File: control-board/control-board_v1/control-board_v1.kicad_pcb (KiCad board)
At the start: 2 copper layers, 68.6 x 53.3 mm, 59 parts, among them J1 Barrel_Jack, J2 PH2-12-UA, J3 PH2-12-UA, J4 PH2-12-UA, J5 PH2-12-UA, J6 Conn_01x08_Socket, J7 Conn_01x06_Socket, J8 Conn_01x10_Socket, J9 Conn_01x08_Socket, Q1 Q_Dual_NMOS_S1G1D2S2G2D1, Q2 Q_Dual_NMOS_S1G1D2S2G2D1, Q3 Q_Dual_NMOS_S1G1D2S2G2D1, Q4 Q_Dual_NMOS_S1G1D2S2G2D1, Q5 Q_Dual_NMOS_S1G1D2S2G2D1, Q6 Q_Dual_NMOS_S1G1D2S2G2D1, Q7 Q_Dual_NMOS_S1G1D2S2G2D1, Q8 Q_Dual_NMOS_S1G1D2S2G2D1, U1 CD74HCT154M, U2 SN74HC540DWR, U3 SN74HC540DWR

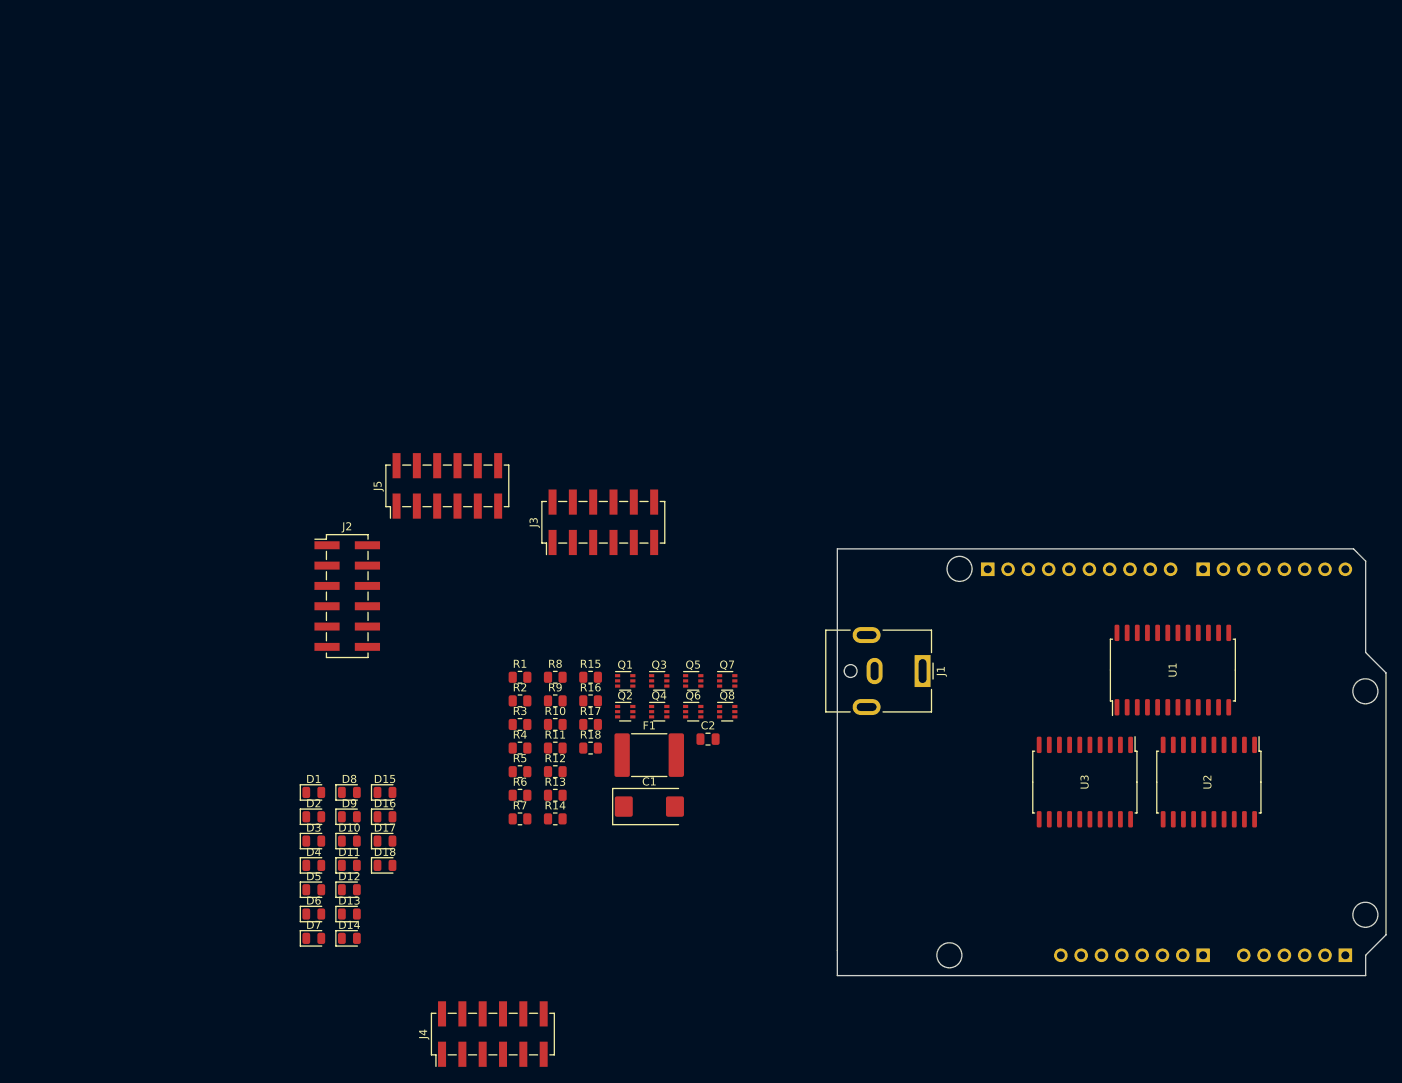
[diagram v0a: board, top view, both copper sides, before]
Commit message: added pcb layout
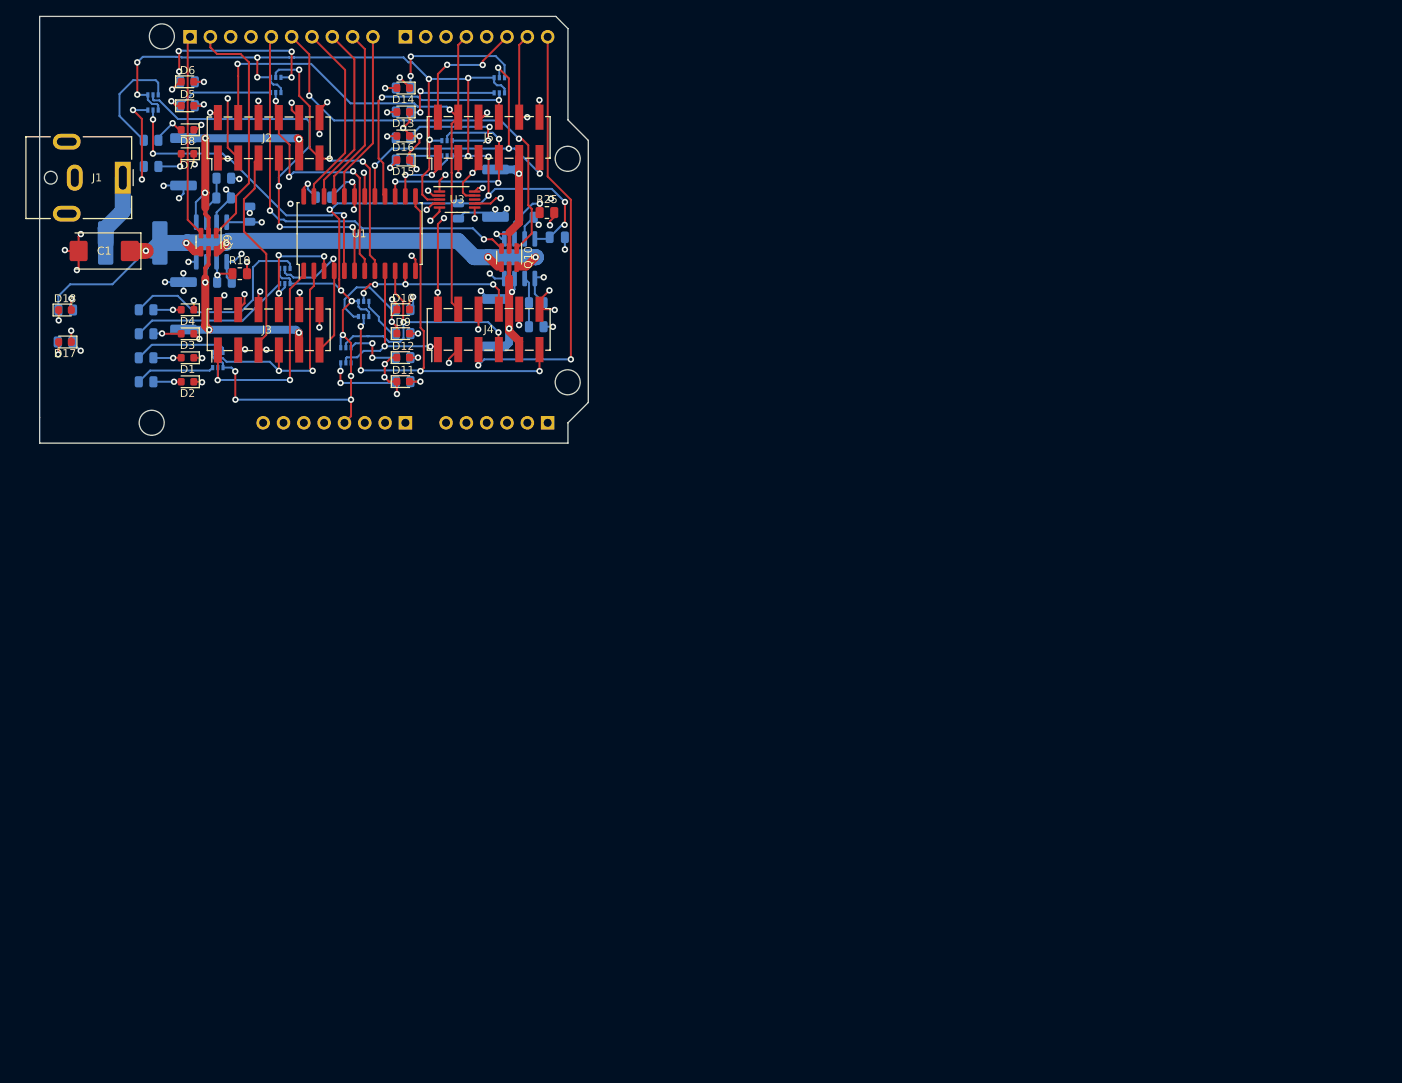
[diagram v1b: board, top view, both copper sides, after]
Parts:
- removed U2: SN74HC540DWR, Package_SO:SOIC-20W_7.5x12.8mm_P1.27mm
- added C3: 0.1uF, Capacitor_SMD:C_0805_2012Metric, B.Cu at (81.5, 42.9)
- added C5: 0.1uF, Capacitor_SMD:C_0805_2012Metric, B.Cu at (69.2, 39.6)
- added C7: 0.1uF, Capacitor_SMD:C_0805_2012Metric, B.Cu at (43.1, 40.0)
- added Q10: NMOS, Package_TO_SOT_SMD:SOT-23-6, F.Cu at (75.5, 45.4)
- added Q9: NMOS, Package_TO_SOT_SMD:SOT-23-6, F.Cu at (38.0, 43.5)
- added R19: 100, Resistor_SMD:R_0805_2012Metric, F.Cu at (41.9, 47.5)
- added R20: 166K, Resistor_SMD:R_0805_2012Metric, B.Cu at (40.0, 48.5)
- added R21: 100, Resistor_SMD:R_0805_2012Metric, B.Cu at (39.9, 35.5)
- added R22: 166K, Resistor_SMD:R_0805_2012Metric, B.Cu at (39.9, 38.0)
- added R23: 0.003, Resistor_SMD:R_2512_6332Metric, B.Cu at (73.8, 53.6)
- added R24: 0.003, Resistor_SMD:R_2512_6332Metric, B.Cu at (73.8, 37.4)
- added R25: 100, Resistor_SMD:R_0805_2012Metric, F.Cu at (80.3, 39.8)
- added R26: 100, Resistor_SMD:R_0805_2012Metric, B.Cu at (78.9, 54.1)
- added R27: 166K, Resistor_SMD:R_0805_2012Metric, B.Cu at (77.7, 40.4)
- added R28: 166K, Resistor_SMD:R_0805_2012Metric, B.Cu at (78.9, 51.1)
- added R42: 0.003, Resistor_SMD:R_2512_6332Metric, B.Cu at (34.8, 51.5)
- added R47: 0.003, Resistor_SMD:R_2512_6332Metric, B.Cu at (34.8, 33.5)
- added U4: Opamp_Dual, Package_SO:SOIC-8_3.9x4.9mm_P1.27mm, B.Cu at (38.3, 43.5)
- added U6: Opamp_Dual, Package_SO:SOIC-8_3.9x4.9mm_P1.27mm, B.Cu at (76.8, 45.6)
- C2, R1, R10, R11, R12, R13, R14, R15, R16, R18, R2, R3, R4, R5, R6, R7, R8, R9: moved to B.Cu
- D1, D17, D2, D3, D4: footprint LED_SMD:LED_0805_2012Metric -> LED_SMD:LED_0603_1608Metric
- D10, D11, D12, D9: value BLUE LED -> RED LED; footprint LED_SMD:LED_0805_2012Metric -> LED_SMD:LED_0603_1608Metric
- D13, D14, D15, D16: value BLUE LED -> YELLOW LED; footprint LED_SMD:LED_0805_2012Metric -> LED_SMD:LED_0603_1608Metric
- D18: value RED LED -> ORANGE LED; footprint LED_SMD:LED_0805_2012Metric -> LED_SMD:LED_0603_1608Metric
- D5, D6, D7, D8: value BLUE LED -> WHITE LED; footprint LED_SMD:LED_0805_2012Metric -> LED_SMD:LED_0603_1608Metric
- F1: value 0ZCF0125FF2C -> Bell_Fuse; moved to B.Cu
- J2, J3, J4, J5: value PH2-12-UA -> Header-M_2x6
- J6, J9: value Conn_01x08_Socket -> Header_1x8
- J7: value Conn_01x06_Socket -> Header_1x8
- J8: value Conn_01x10_Socket -> Header_1x10
- Q1, Q2, Q3, Q4, Q5, Q6, Q7, Q8: value Q_Dual_NMOS_S1G1D2S2G2D1 -> PMOS; moved to B.Cu
- R17: value 1K -> 100; moved to B.Cu
- U3: value SN74HC540DWR -> ADS1118; footprint Package_SO:SOIC-20W_7.5x12.8mm_P1.27mm -> Package_SO:VSSOP-10_3x3mm_P0.5mm
- moved J6 119.9 mm to (62.6, 66.1)
- moved J7 119.9 mm to (80.3, 66.1)
- moved J8 119.9 mm to (35.6, 17.8)
- moved J9 119.9 mm to (62.6, 17.8)
- moved J1 117.5 mm to (27.2, 35.5)
- moved U1 115.4 mm to (56.8, 42.4)
- moved U3 107.1 mm to (69.0, 38.2), turned to 0 degrees
- moved D14 106.5 mm to (62.3, 24.2), turned to 180 degrees
- moved D6 105.2 mm to (35.3, 23.5)
- moved D13 100.5 mm to (62.3, 27.2), turned to 180 degrees
- moved D7 99.3 mm to (35.3, 32.5), turned to 180 degrees
- moved D5 99.3 mm to (35.3, 26.5)
- moved Q4 99.0 mm to (31.0, 26.1), turned to 90 degrees
- moved R6 98.4 mm to (35.3, 23.5)
- moved C1 97.3 mm to (24.9, 44.6), turned to 180 degrees
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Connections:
- net D10 renamed S-D10
- net D11 renamed S-D11
- net D8 renamed S-D8
- net D9 renamed S-D9
- C2 pad 2: +5V -> +3V3
- D1 pad 1: Net-(D1-K) -> GND
- D10 pad 1: Net-(D10-K) -> GND
- D11 pad 1: Net-(D11-K) -> GND
- D12 pad 1: Net-(D12-K) -> GND
- D13 pad 1: Net-(D13-K) -> GND
- D14 pad 1: Net-(D14-K) -> GND
- D15 pad 1: Net-(D15-K) -> GND
- D16 pad 1: Net-(D16-K) -> GND
- D2 pad 1: Net-(D2-K) -> GND
- D3 pad 1: Net-(D3-K) -> GND
- D4 pad 1: Net-(D4-K) -> GND
- D5 pad 1: Net-(D5-K) -> GND
- D6 pad 1: Net-(D6-K) -> GND
- D7 pad 1: Net-(D7-K) -> GND
- D8 pad 1: Net-(D8-K) -> GND
- D9 pad 1: Net-(D9-K) -> GND
- J1 pad MP: (no net) -> GND
- J2 pad 9: +9V -> 2-Heater
- J3 pad 9: +9V -> 1-Heater
- J4 pad 9: +9V -> 3-Heater
- J5 pad 5: unconnected-(J5-Pin_5-Pad5) -> DOUT
- J5 pad 9: +9V -> 4-Heater
- J8 pad 1: SCL -> H2-D13
- J8 pad 2: SDA -> H1-D12
- J8 pad 5: D13 -> H4-D19
- J8 pad 6: D12 -> H3-D18
- J9 pad 2: D6 -> ~{ENABLE}
- J9 pad 5: D3 -> CS
- J9 pad 6: CLK -> DIN
- J9 pad 7: DIN -> CLK
- Q1 pad 1: Inv_4T1 -> +5V
- Q1 pad 2: GND -> 1-CS
- Q1 pad 3: Net-(D2-K) -> Net-(Q1B-D)
- Q1 pad 4: Inv_4 -> +5V
- Q1 pad 5: GND -> 1-CS_T1
- Q1 pad 6: Net-(D1-K) -> Net-(Q1A-D)
- Q2 pad 1: Inv_3T3 -> +5V
- Q2 pad 2: GND -> 1-CS_T2
- Q2 pad 3: Net-(D3-K) -> Net-(Q2B-D)
- Q2 pad 4: Inv_3T2 -> +5V
- Q2 pad 5: GND -> 1-CS_T3
- Q2 pad 6: Net-(D4-K) -> Net-(Q2A-D)
- Q3 pad 1: Inv_3T1 -> +5V
- Q3 pad 2: GND -> 2-CS_T2
- Q3 pad 3: Net-(D5-K) -> Net-(Q3B-D)
- Q3 pad 4: Inv_3 -> +5V
- Q3 pad 5: GND -> 2-CS_T3
- Q3 pad 6: Net-(D6-K) -> Net-(Q3A-D)
- Q4 pad 1: Inv_2T3 -> +5V
- Q4 pad 2: GND -> 2-CS
- Q4 pad 3: Net-(D9-K) -> Net-(Q4B-D)
- Q4 pad 4: Inv_2T2 -> +5V
- Q4 pad 5: GND -> 2-CS_T1
- Q4 pad 6: Net-(D7-K) -> Net-(Q4A-D)
- Q5 pad 1: Inv_2T1 -> +5V
- Q5 pad 2: GND -> 3-CS_T2
- Q5 pad 3: Net-(D11-K) -> Net-(Q5B-D)
- Q5 pad 4: Inv_2 -> +5V
- Q5 pad 5: GND -> 3-CS_T3
- Q5 pad 6: Net-(D8-K) -> Net-(Q5A-D)
- Q6 pad 1: Inv_1T3 -> +5V
- Q6 pad 2: GND -> 3-CS
- Q6 pad 3: Net-(D12-K) -> Net-(Q6B-D)
- Q6 pad 4: Inv_1T2 -> +5V
- Q6 pad 5: GND -> 3-CS_T1
- Q6 pad 6: Net-(D10-K) -> Net-(Q6A-D)
- Q7 pad 1: Inv_4T3 -> +5V
- Q7 pad 2: GND -> 4-CS_T2
- Q7 pad 3: Net-(D14-K) -> Net-(Q7B-D)
- Q7 pad 4: Inv_4T2 -> +5V
- Q7 pad 5: GND -> 4-CS_T3
- Q7 pad 6: Net-(D13-K) -> Net-(Q7A-D)
- Q8 pad 1: Inv_1T1 -> +5V
- Q8 pad 2: GND -> 4-CS
- Q8 pad 3: Net-(D16-K) -> Net-(Q8B-D)
- Q8 pad 4: Inv_1 -> +5V
- Q8 pad 5: GND -> 4-CS_T1
- Q8 pad 6: Net-(D15-K) -> Net-(Q8A-D)
- R1 pad 1: +5V -> Net-(Q1A-D)
- R10 pad 1: +5V -> Net-(Q5A-D)
- R11 pad 1: +5V -> Net-(Q6B-D)
- R12 pad 1: +5V -> Net-(Q6A-D)
- R13 pad 1: +5V -> Net-(Q7B-D)
- R14 pad 1: +5V -> Net-(Q7A-D)
- R15 pad 1: +5V -> Net-(Q8B-D)
- R16 pad 1: +5V -> Net-(Q8A-D)
- R17 pad 1: +5V -> +3V3
- R2 pad 1: +5V -> Net-(Q1B-D)
- R3 pad 1: +5V -> Net-(Q2B-D)
- R4 pad 1: +5V -> Net-(Q2A-D)
- R5 pad 1: +5V -> Net-(Q3B-D)
- R6 pad 1: +5V -> Net-(Q3A-D)
- R7 pad 1: +5V -> Net-(Q4B-D)
- R8 pad 1: +5V -> Net-(Q4A-D)
- R9 pad 1: +5V -> Net-(Q5B-D)
- U1 pad 18: GND -> ~{ENABLE}
- U1 pad 24: +5V -> +3V3
- U3 pad 1: GND -> CLK
- U3 pad 10: GND -> DIN
- U3 pad 2: 2-CS_T3 -> CS
- U3 pad 3: 2-CS_T2 -> +5V
- U3 pad 4: 2-CS_T1 -> /current-sensing/V_{h1}
- U3 pad 5: 2-CS -> /current-sensing/V_{h2}
- U3 pad 6: 1-CS_T3 -> /current-sensing/V_{h4}
- U3 pad 7: 1-CS_T2 -> /current-sensing/V_{h3}
- U3 pad 8: 1-CS_T1 -> (no net)
- U3 pad 9: 1-CS -> DOUT
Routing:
- net +5V: track 0.00 -> 222.0 mm, vias 0 -> 21
- net DOUT: track 0.00 -> 145.1 mm, vias 0 -> 4
- net ~{RDY}: track 0.00 -> 119.1 mm, vias 0 -> 4
- net DIN: track 0.00 -> 118.1 mm, vias 0 -> 7
- net CLK: track 0.00 -> 113.5 mm, vias 0 -> 5
- net ~{RST}: track 0.00 -> 105.5 mm, vias 0 -> 3
- net GND: track 0.00 -> 94.7 mm, vias 0 -> 47
- net +9V: track 0.00 -> 75.0 mm, vias 0 -> 5
- net 3-CS_T3: track 0.00 -> 54.4 mm, vias 0 -> 4
- net 2-CS_T1: track 0.00 -> 54.3 mm, vias 0 -> 3
- net H4-D19: track 0.00 -> 52.7 mm, vias 0 -> 2
- net H3-D18: track 0.00 -> 52.1 mm, vias 0 -> 2
- net 2-CS: track 0.00 -> 41.0 mm, vias 0 -> 4
- net 4-CS_T3: track 0.00 -> 40.6 mm, vias 0 -> 4
- net /current-sensing/V_{h2}: track 0.00 -> 35.7 mm, vias 0 -> 2
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- added copper zone on In2.Cu, net +3V3
- added copper zone on In1.Cu, net GND
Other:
- outline, holes or cut-outs redrawn
- copper layers 2 -> 4

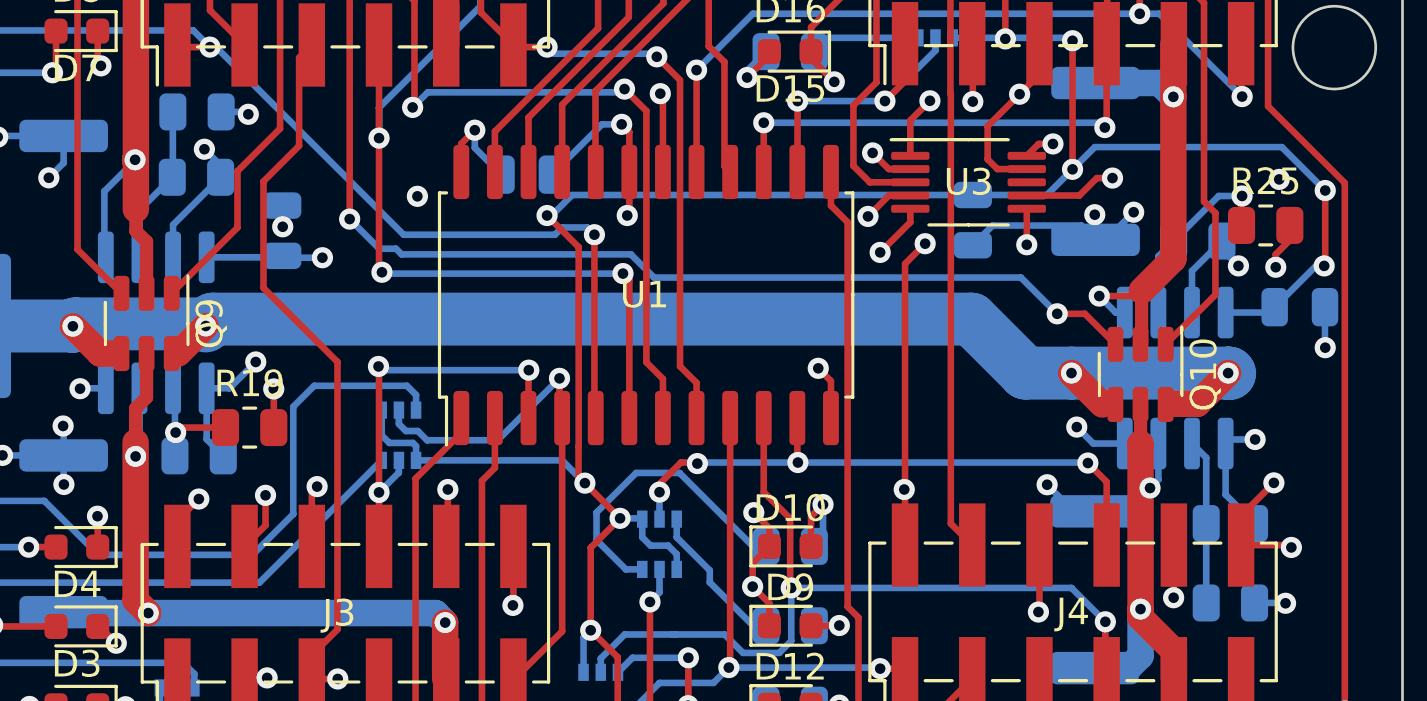
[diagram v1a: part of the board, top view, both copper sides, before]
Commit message: added datasheets
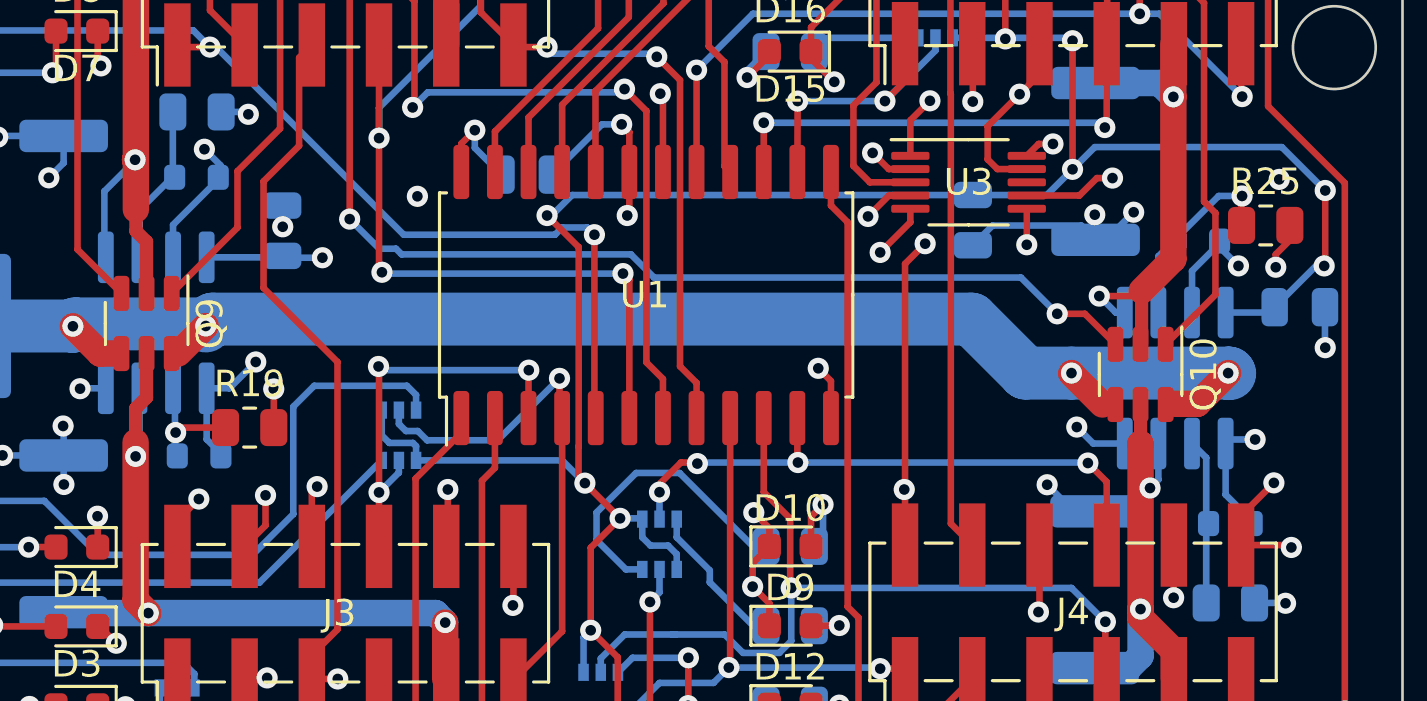
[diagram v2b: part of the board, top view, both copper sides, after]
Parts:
- R20, R22, R27, R28: footprint Resistor_SMD:R_0805_2012Metric -> Resistor_SMD:R_0603_1608Metric

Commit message: pcb design change
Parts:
- C3, C5, C7, R21, R26: moved to F.Cu
- U3: moved to B.Cu
- moved Q3 38.1 mm to (46.2, 62.0), turned to -90 degrees
- moved Q4 37.2 mm to (41.7, 61.7), turned to 180 degrees
- moved D6 30.5 mm to (35.3, 54.0), turned to 180 degrees
- moved R6 30.5 mm to (35.3, 54.0), turned to 180 degrees
- moved R2 30.4 mm to (35.3, 31.0), turned to 180 degrees
- moved R3 30.4 mm to (35.3, 25.0), turned to 180 degrees
- moved D8 30.3 mm to (35.3, 59.8)
- moved D2 30.0 mm to (35.3, 31.0)
- moved D3 30.0 mm to (35.3, 25.0)
- moved R8 29.4 mm to (35.3, 59.8), turned to 180 degrees
- moved R42 27.3 mm to (48.6, 27.9), turned to 0 degrees
- moved D5 24.5 mm to (35.3, 51.0), turned to 180 degrees
- moved R5 24.5 mm to (35.3, 51.0), turned to 180 degrees
- moved R1 24.5 mm to (35.3, 34.0), turned to 180 degrees
- moved R4 24.5 mm to (35.3, 28.0), turned to 180 degrees
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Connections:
- J1 pad MP: GND -> (no net)
- J2 pad 12: GND -> 2-GND
- J3 pad 12: GND -> 1-GND
- J4 pad 12: GND -> 3-GND
- J5 pad 12: GND -> 4-GND
- J8 pad 1: H2-D13 -> H1-D12
- J8 pad 2: H1-D12 -> H2-D13
- J9 pad 6: DIN -> CLK
- J9 pad 7: CLK -> DIN
- R23 pad 2: 3-Heater -> 3-GND
- R24 pad 2: 4-Heater -> 4-GND
- R42 pad 2: 1-Heater -> 1-GND
- R47 pad 2: 2-Heater -> 2-GND
- U4 pad 3: 1-Heater -> 1-GND
- U4 pad 5: 2-Heater -> 2-GND
- U6 pad 3: 3-Heater -> 3-GND
- U6 pad 5: 4-Heater -> 4-GND
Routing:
- net +5V: track 222.0 -> 174.5 mm, vias 21 -> 6
- net GND: track 94.7 -> 123.8 mm, vias 47 -> 46
- net 1-GND: track 0.00 -> 22.0 mm, vias 0 -> 3
- net 1-Heater: track 29.6 -> 8.89 mm, vias 3 -> 0
- net 4-GND: track 0.00 -> 20.5 mm, vias 0 -> 3
- net /current-sensing/V_{h1}: track 34.9 -> 54.9 mm
- net 2-Heater: track 33.0 -> 13.9 mm, vias 3 -> 0
- net 2-CS_T1: track 54.3 -> 38.8 mm, vias 3 -> 4
- net /current-sensing/V_{h4}: track 14.1 -> 28.5 mm
- net 3-GND: track 0.00 -> 14.2 mm, vias 0 -> 3
- net 2-GND: track 0.00 -> 14.0 mm, vias 0 -> 3
- net H2-D13: track 25.3 -> 39.2 mm, vias 0 -> 1
- net /current-sensing/V_{h2}: track 35.7 -> 48.8 mm, vias 2 -> 3
- net Net-(Q2A-D): track 26.2 -> 13.5 mm
- net Net-(Q8A-D): track 16.6 -> 3.87 mm, vias 2 -> 0
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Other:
- board text added: "(\__/) ( •-•) / >"
- board text added: "1"
- board text added: "2"
- board text added: "3"
- board text added: "4"
- board text added: "9V Heaters"
- board text added: "CS_T3 CS_T2 CS_T1 CS"
- board text added: "Control Board v1 Boston University N. Gonzalez 06-2024"
- board text added: "DIN ~{RST} 3V3 ~{CS_T2} CLK GND"
- board text added: "Heaters Power"
- board text added: "TM NUM"
- board text added: "TMs Power"
- board text added: "~{CS} ~{RDY} DOUT ~{CS_T1} VCC ~{CS_T3}"
